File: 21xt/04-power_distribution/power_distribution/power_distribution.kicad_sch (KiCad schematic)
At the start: 29 parts, among them J1 Conn_01x02, J2 Conn_01x02, J3 Conn_01x02, Q1 NMOS, Q2 NMOS, U1 LM74700, U2 XIAO-ESP32-C3-DIP, U3 LM74700, U4 INA180A1, U5 LTC2959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

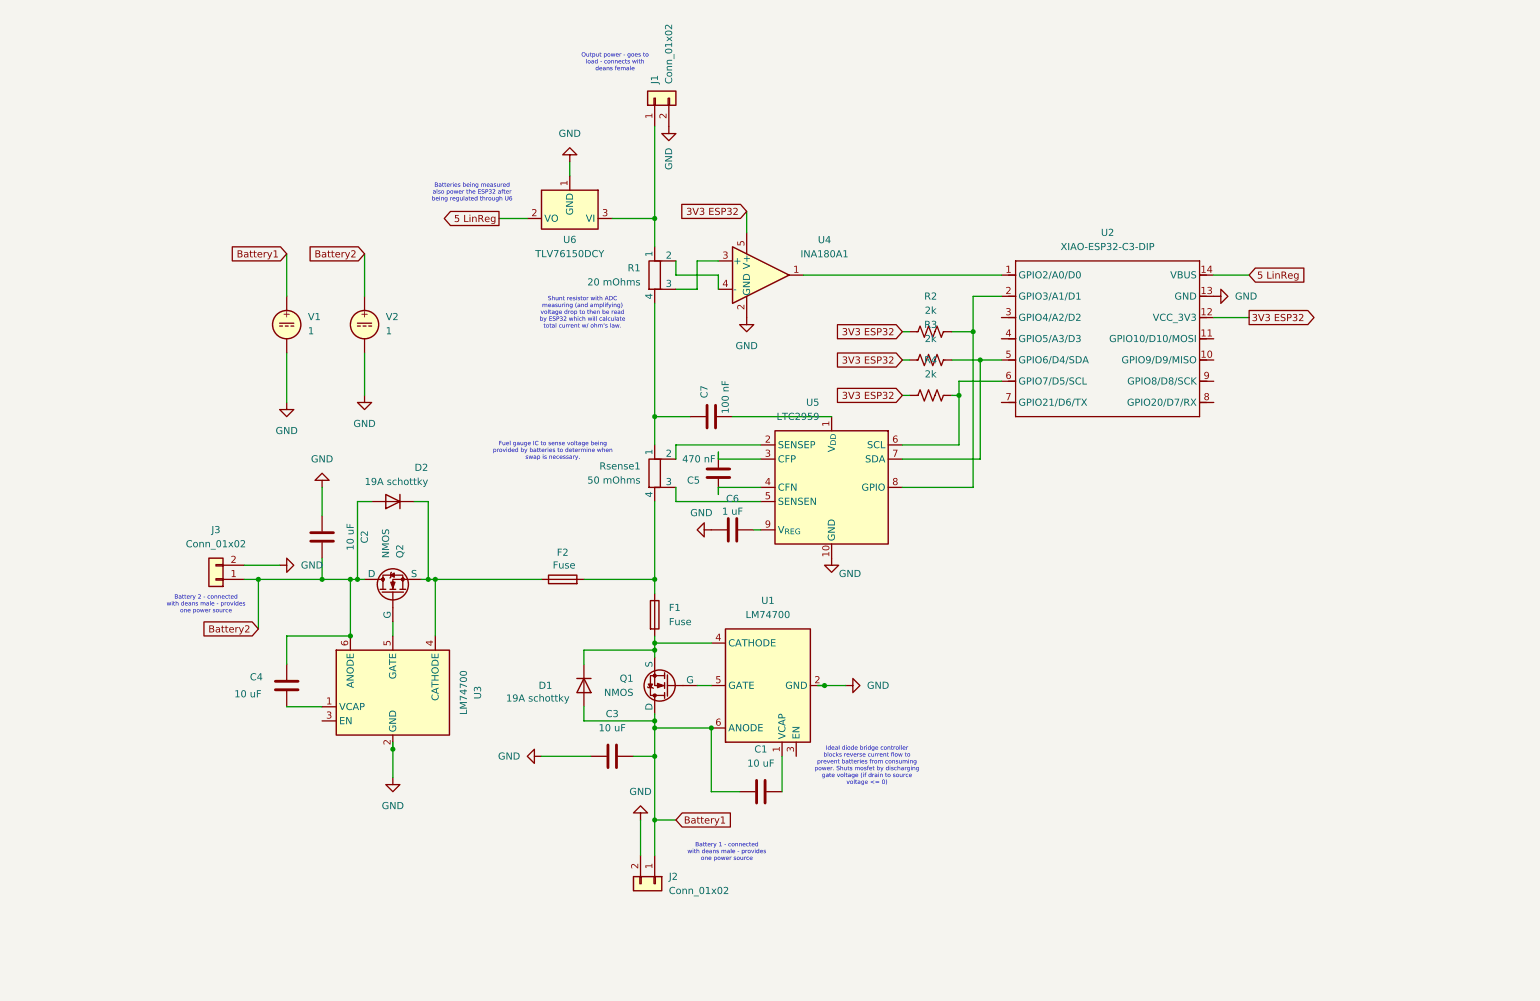
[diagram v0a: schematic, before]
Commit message: altered one battery connection
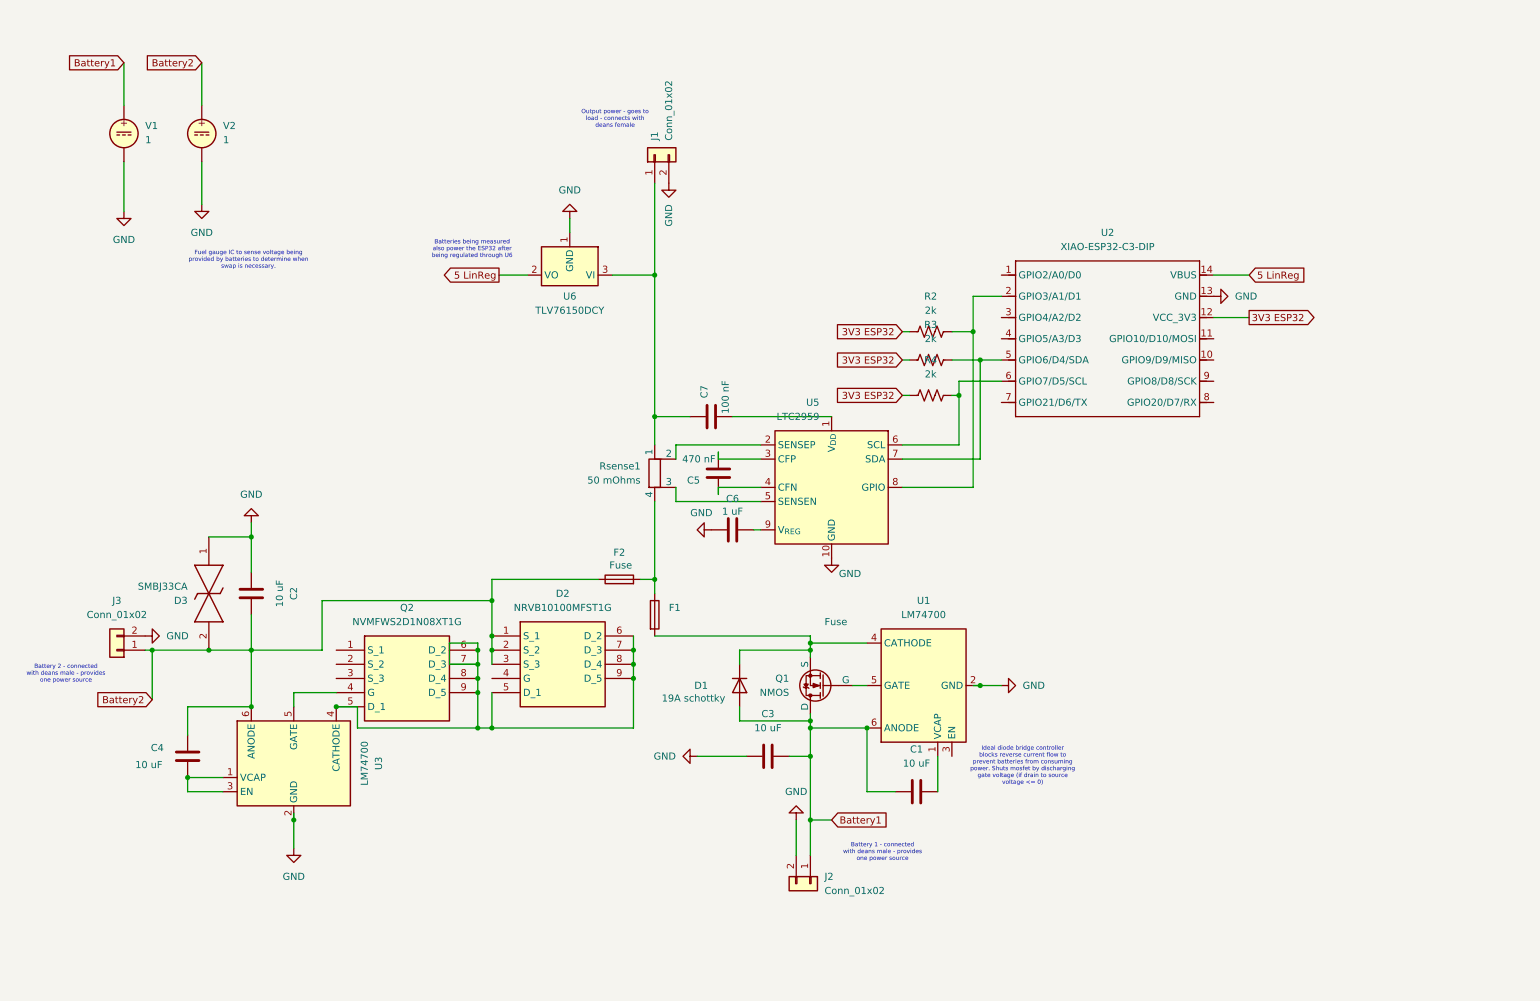
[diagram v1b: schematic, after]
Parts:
- removed D2: 19A schottky, Package_TO_SOT_THT:TO-220-2_Vertical, symbol Device:D
- removed Q2: NMOS, Package_TO_SOT_SMD:TO-263-2, symbol Simulation_SPICE:NMOS
- removed R1: 20 mOhms, Resistor_SMD:R_0402_1005Metric, symbol Device:R_Shunt
- removed U4: INA180A1, Package_TO_SOT_SMD:SOT-23-5, symbol Amplifier_Current:INA180A1
- added D2: NRVB10100MFST1G, 21xt_footprints:NRVTS10100EMFST1G, symbol 21xt_symbols:NRVB10100MFST1G
- added D3: SMBJ33CA, 21xt_footprints:SMBJ33CA, symbol 21xt_symbols:SMBJ33CA
- added Q2: NVMFWS2D1N08XT1G, 21xt_footprints:NTMFWS1D5N08XT1G, symbol 21xt_symbols:NVMFWS2D1N08XT1G
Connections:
- net Battery2: now also F2.1, D2.1 (S_1), D2.2 (S_2), D2.3 (S_3), D3.2
- net GND: now also D3.1
- net at C7.2, Rsense1.1: now also J1.1 (Pin_1), U6.3 (VI)
- net at C4.1, U3.1 (VCAP): now also U3.3 (EN)
- net at U3.4 (CATHODE): now also D2.5 (D_1), D2.6 (D_2), D2.7 (D_3), D2.8 (D_4), D2.9 (D_5), Q2.5 (D_1), Q2.6 (D_2), Q2.7 (D_3), Q2.8 (D_4), Q2.9 (D_5); no longer F2.1
- net at U3.5 (GATE): now also Q2.4 (G)
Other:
- note removed: "Shunt resistor with ADC measuring (and amplifying) voltage drop to then be read by ESP32 which will calculate total current w/ ohm's law."
- moved on the sheet: C1, C2, C3, C4, D1, F2, J1, J2, J3, Q1, U1, U3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

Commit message: redone schematic
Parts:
- removed C1, C3: 10 uF, Capacitor_SMD:C_0201_0603Metric, symbol Device:C
- removed D1: 19A schottky, Package_TO_SOT_THT:TO-220-2_Vertical, symbol Device:D
- removed J2: Conn_01x02, 21xt_footprints:Deans Connector Male, symbol Connector_Generic:Conn_01x02
- removed Q1: NMOS, Package_TO_SOT_SMD:TO-263-2, symbol Simulation_SPICE:NMOS
- removed U1: LM74700, Package_TO_SOT_SMD:SOT-23-6, symbol Power_Management:LM74700
- added C10: 100uF, Capacitor_SMD:C_0603_1608Metric, symbol Device:C
- added C8, C9: 10 uF, Capacitor_SMD:C_0201_0603Metric, symbol Device:C
- added D4: SMBJ33CA, 21xt_footprints:SMBJ33CA, symbol 21xt_symbols:SMBJ33CA
- added D5: NRVB10100MFST1G, 21xt_footprints:NRVTS10100EMFST1G, symbol 21xt_symbols:NRVB10100MFST1G
- added J4: Conn_01x02, 21xt_footprints:Deans Connector Male, symbol Connector_Generic:Conn_01x02
- added Q3: NVMFWS2D1N08XT1G, 21xt_footprints:NTMFWS1D5N08XT1G, symbol 21xt_symbols:NVMFWS2D1N08XT1G
- added U4: LM74700, Package_TO_SOT_SMD:SOT-23-6, symbol Power_Management:LM74700
- C7: value 100 nF -> 10uF; footprint Capacitor_SMD:C_0201_0603Metric -> Capacitor_SMD:C_0402_1005Metric
- R2, R3, R4: footprint (none) -> Resistor_SMD:R_0402_1005Metric
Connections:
- net 3V3 ESP32: now also U5.8 (GPIO)
- net 5 LinReg: now also U5.1 (V_{DD})
- net Battery1: now also C8.2, C9.2, D4.2, D5.1 (S_1), D5.2 (S_2), D5.3 (S_3), J4.1 (Pin_1), U4.6 (ANODE)
- net Battery2: no longer F2.1
- net GND: now also C7.2, C10.2, C9.1, D4.1, J4.2 (Pin_2), U4.2 (GND)
- net Battery1_Supply: now reaches F1.2
- net Battery1_Supply: now also D5.5 (D_1), D5.6 (D_2), D5.7 (D_3), D5.8 (D_4), D5.9 (D_5), Q3.5 (D_1), Q3.6 (D_2), Q3.7 (D_3), Q3.8 (D_4), Q3.9 (D_5), U4.4 (CATHODE)
- net at J1.1 (Pin_1), Rsense1.1, U6.3 (VI): now also C10.1; no longer C7.2
- net at F1.1, F2.2, Rsense1.4: now also C7.1
- net at R2.2, U2.2 (GPIO3/A1/D1): no longer U5.8 (GPIO)
- net Battery2_Supply: now reaches D2.5 (D_1), D2.6 (D_2), D2.7 (D_3), D2.8 (D_4), D2.9 (D_5), Q2.5 (D_1), Q2.6 (D_2), Q2.7 (D_3), Q2.8 (D_4), Q2.9 (D_5), U3.4 (CATHODE)
- net Battery2_Supply: now also F2.1
- net SCL: now reaches R4.2, U2.6 (GPIO7/D5/SCL), U5.6 (SCL)
- net SDA: now reaches R3.2, U2.5 (GPIO6/D4/SDA), U5.7 (SDA)
- new net: Q3.4 (G), U4.5 (GATE)
- new net: C8.1, U4.1 (VCAP), U4.3 (EN)
- no-connect marks 0 -> 20
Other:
- moved on the sheet: C2, C4, C5, C6, D2, D3, F1, F2, J1, J3, Q2, R2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

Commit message: saving progress on pcb layout rework
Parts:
- U2: footprint ESP32C:XIAO-ESP32C3-DIP -> 21xt_footprints:esp32 c6 xiao
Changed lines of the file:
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@@
 			)
 		)
-		(property "Footprint" "ESP32C:XIAO-ESP32C3-DIP"
+		(property "Footprint" "21xt_footprints:esp32 c6 xiao"
 			(at 230.124 57.404 0)
 			(effects

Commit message: PCB layed out
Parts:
- removed F1: Fuse, Fuse:Fuseholder_Cylinder-5x20mm_Stelvio-Kontek_PTF78_Horizontal_Open, symbol Device:Fuse
- F2: footprint Fuse:Fuseholder_Cylinder-5x20mm_Stelvio-Kontek_PTF78_Horizontal_Open -> Fuse:Fuse_1206_3216Metric_Pad1.42x1.75mm_HandSolder
- Rsense1: footprint Resistor_SMD:R_0402_1005Metric -> Resistor_SMD:R_1206_3216Metric
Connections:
- net Battery2_Supply is gone; now on net Battery1_Supply: D2.5 (D_1), D2.6 (D_2), D2.7 (D_3), D2.8 (D_4), D2.9 (D_5), F2.1, Q2.5 (D_1), Q2.6 (D_2), Q2.7 (D_3), Q2.8 (D_4), Q2.9 (D_5), U3.4 (CATHODE)
- no-connect marks 20 -> 16
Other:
- moved on the sheet: C2, C4, C8, C9, D2, D3, D4, D5, F2, J3, J4, Q2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
